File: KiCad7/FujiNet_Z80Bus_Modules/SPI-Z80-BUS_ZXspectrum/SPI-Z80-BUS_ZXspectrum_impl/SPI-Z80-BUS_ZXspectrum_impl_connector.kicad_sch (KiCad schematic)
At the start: 8 parts, among them J1 PinHeader_2.54mm, J2 Z80_CONTROL

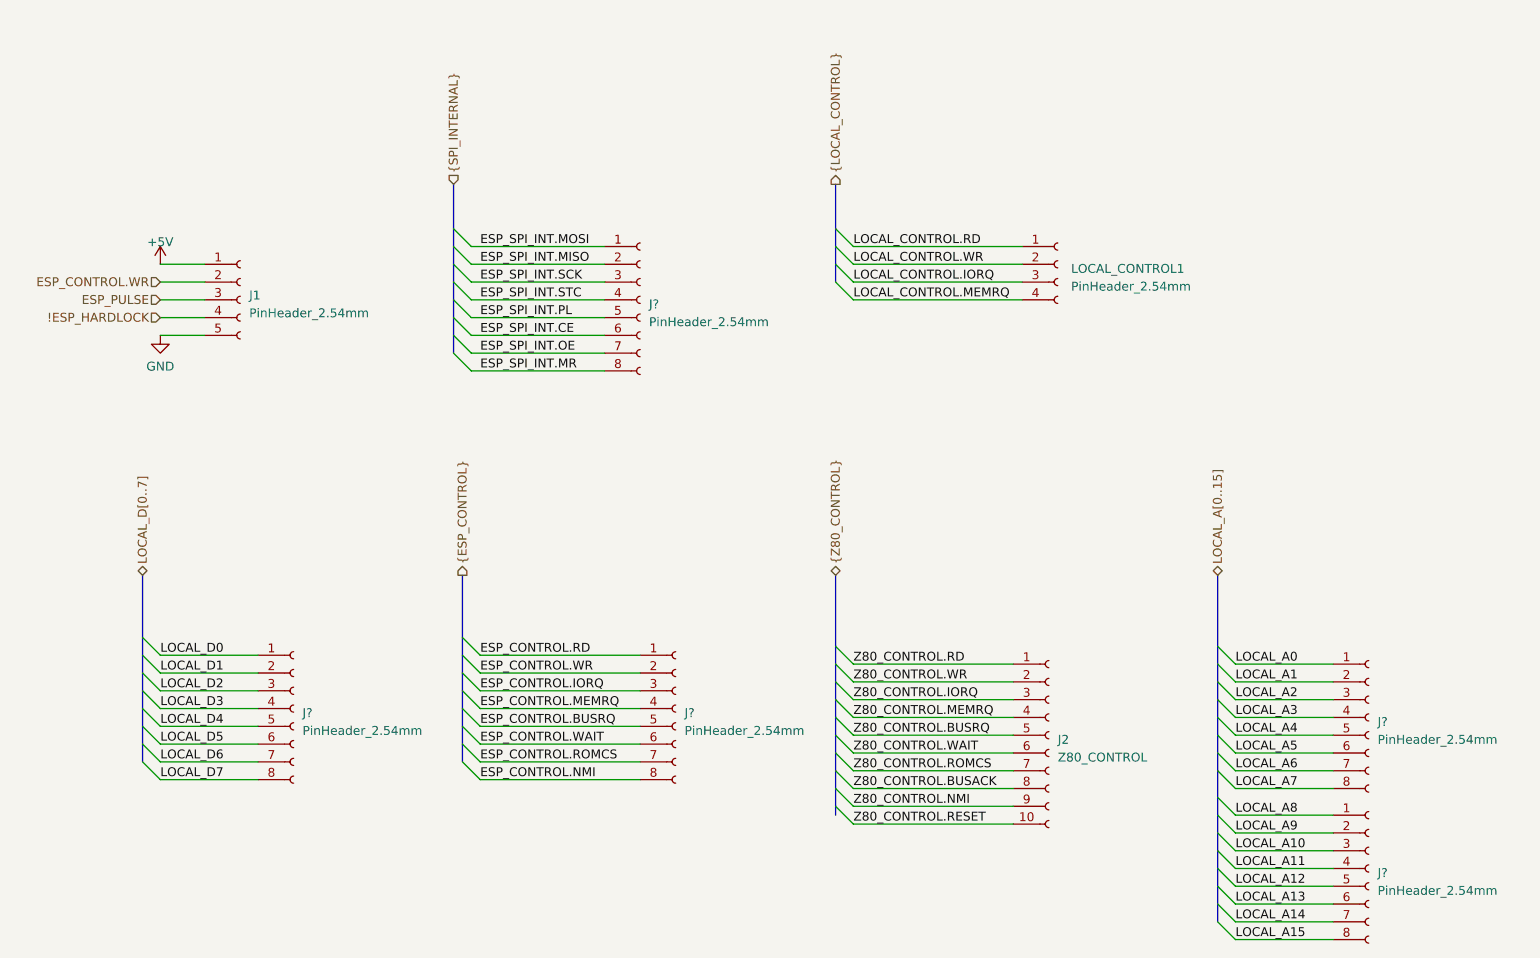
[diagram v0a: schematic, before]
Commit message: KICad fixed SPI impl
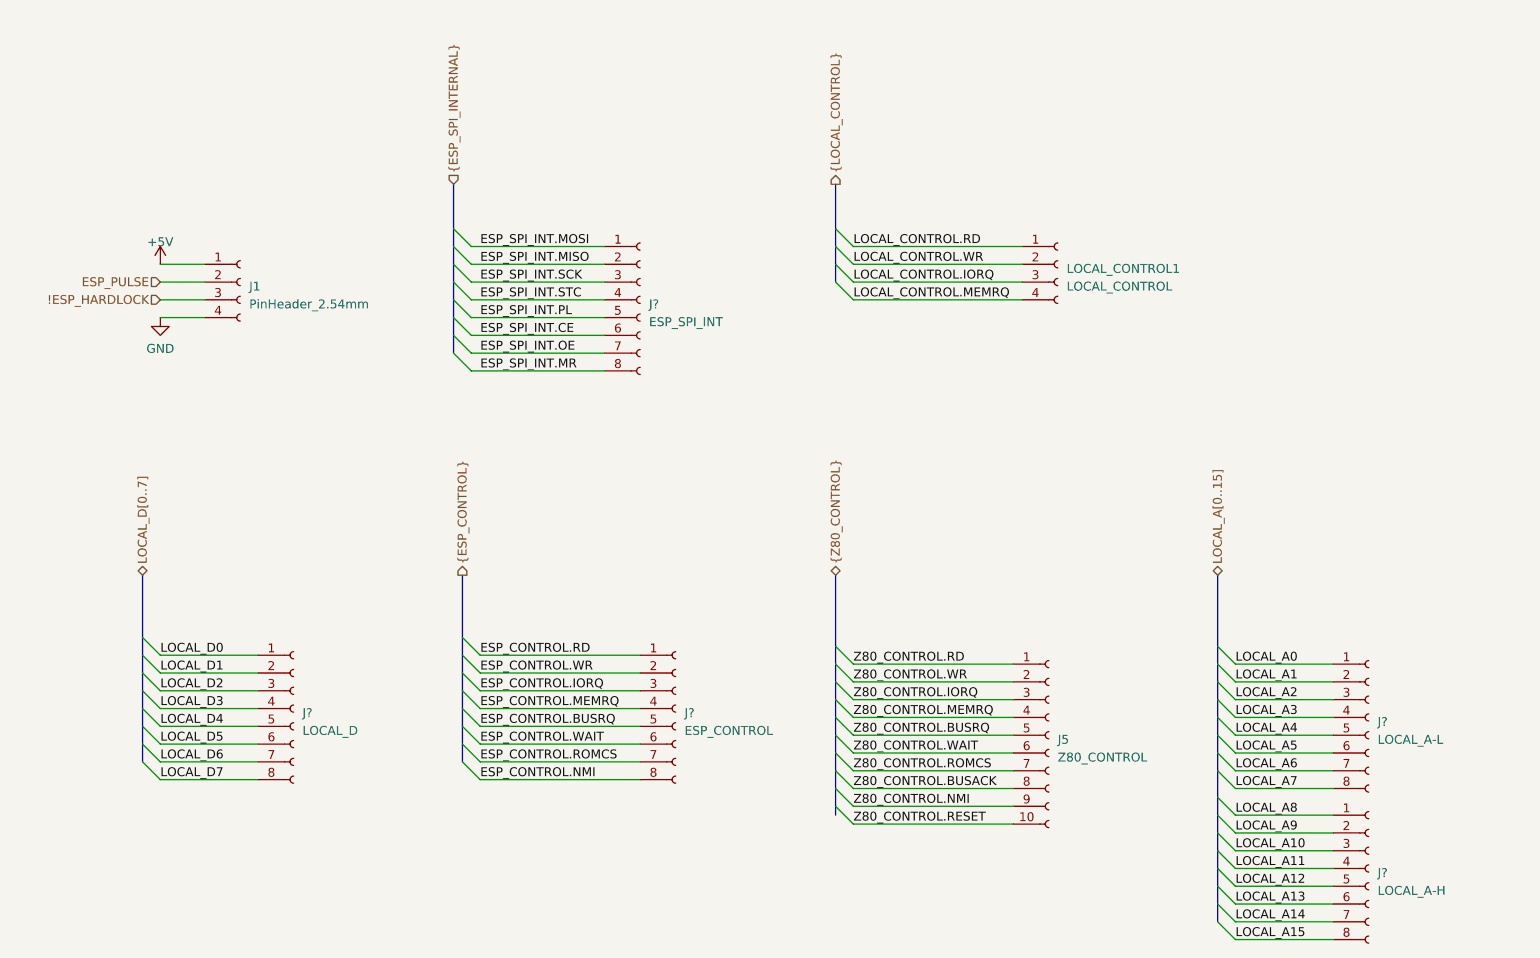
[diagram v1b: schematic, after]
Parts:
- removed J1: PinHeader_2.54mm, Connector_PinHeader_2.54mm:PinHeader_1x05_P2.54mm_Vertical, symbol Connector:Conn_01x05_Socket
- added J1: PinHeader_2.54mm, Connector_PinHeader_2.54mm:PinHeader_1x04_P2.54mm_Vertical, symbol Connector:Conn_01x04_Socket
- J?: value PinHeader_2.54mm -> LOCAL_D
- J?: value PinHeader_2.54mm -> ESP_CONTROL
- J?: value PinHeader_2.54mm -> LOCAL_A-L
- J?: value PinHeader_2.54mm -> LOCAL_A-H
- J?: value PinHeader_2.54mm -> ESP_SPI_INT
- LOCAL_CONTROL1: value PinHeader_2.54mm -> LOCAL_CONTROL
- renumbered J2 to J5
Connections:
- net !ESP_HARDLOCK: now also J1.3 (Pin_3)
- net +5V: now also J1.1 (Pin_1)
- net ESP_PULSE: now also J1.2 (Pin_2)
- net GND: now also J1.4 (Pin_4)
